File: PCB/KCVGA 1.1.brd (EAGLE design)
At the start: 50 x 50 mm, 61 parts, among them IC1 M68AW128MND, IC2 74245ADB, IC4 LD117AS12TR, IC5 LD117AS33TR, U1 XC3S50ATQ144, U2 PIC32MX250F128B_I_SS, U3 PIC32MX270F256D, X1 D-SUB15, X2 MINI-USB

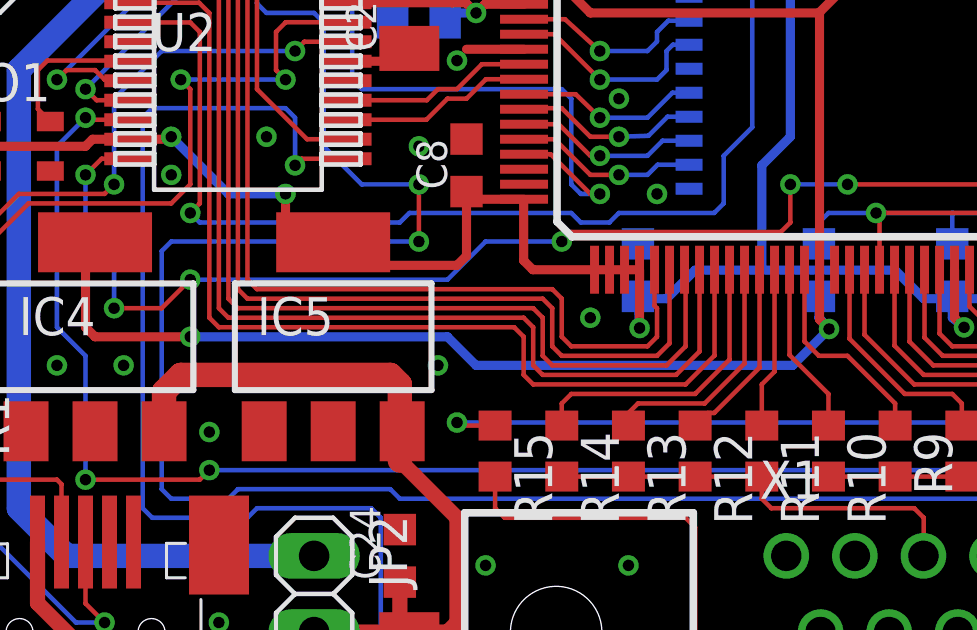
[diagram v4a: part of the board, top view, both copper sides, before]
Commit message: added LDO output caps added Eagle3d files
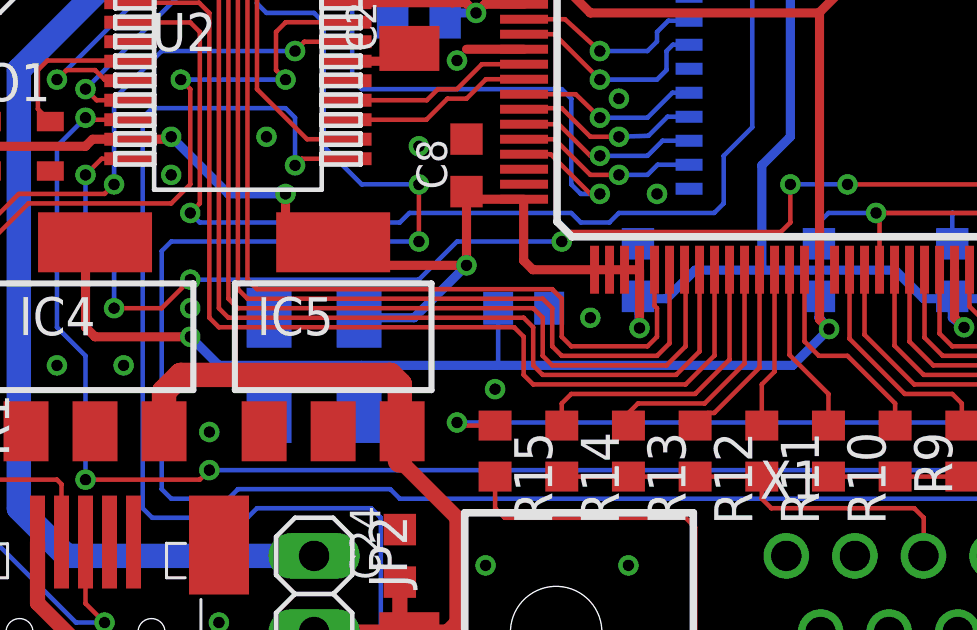
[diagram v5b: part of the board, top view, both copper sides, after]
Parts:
- added C25, C26: 10u, rcl:C1206K
- added R22: 120, rcl:R0603
- IC4: value LD117AS12TR -> LD117AS12
- IC5: value LD117AS33TR -> LD117AS33
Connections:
- net 3V3: now also C26.1
- net GND: now also C25.2, C26.2, R22.1
- net VCCINT: now also C25.1, R22.2
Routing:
- net 3V3: track 237.7 -> 242.2 mm, vias 17 -> 18
- net VCCINT: track 83.1 -> 86.6 mm
- net GND: vias 49 -> 50
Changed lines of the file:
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@@
 <setting verticaltext="up"/>
 </settings>
-<grid distance="12.5" unitdist="mil" unit="mil" style="lines" multiple="1" display="yes" altdistance="1" altunitdist="mil" altunit="mil"/>
+<grid distance="12.5" unitdist="mil" unit="mil" style="lines" multiple="1" display="yes" altdistance="6.25" altunitdist="mil" altunit="mil"/>
 <layers>
 <layer number="1" name="Top" color="4" fill="1" visible="yes" active="yes"/>
@@
 <layer number="19" name="Unrouted" color="6" fill="1" visible="yes" active="yes"/>
 <layer number="20" name="Dimension" color="15" fill="1" visible="yes" active="yes"/>
-<layer number="21" name="tPlace" color="7" fill="1" visible="yes" active="yes"/>
-<layer number="22" name="bPlace" color="7" fill="1" visible="no" active="yes"/>
-<layer number="23" name="tOrigins" color="15" fill="1" visible="yes" active="yes"/>
-<layer number="24" name="bOrigins" color="15" fill="1" visible="no" active="yes"/>
+<layer number="21" name="tPlace" color="7" fill="1" visible="no" active="yes"/>
+<layer number="22" name="bPlace" color="7" fill="1" visible="yes" active="yes"/>
+<layer number="23" name="tOrigins" color="15" fill="1" visible="no" active="yes"/>
+<layer number="24" name="bOrigins" color="15" fill="1" visible="yes" active="yes"/>
 <layer number="25" name="tNames" color="7" fill="1" visible="no" active="yes"/>
 <layer number="26" name="bNames" color="7" fill="1" visible="no" active="yes"/>
@@
 <layer number="49" name="Reference" color="7" fill="1" visible="yes" active="yes"/>
 <layer number="50" name="dxf" color="7" fill="1" visible="no" active="no"/>
-<layer number="51" name="tDocu" color="7" fill="1" visible="yes" active="yes"/>
-<layer number="52" name="bDocu" color="7" fill="1" visible="no" active="yes"/>
+<layer number="51" name="tDocu" color="7" fill="1" visible="no" active="yes"/>
+<layer number="52" name="bDocu" color="7" fill="1" visible="yes" active="yes"/>
 <layer number="90" name="Modules" color="5" fill="1" visible="no" active="no"/>
 <layer number="91" name="Nets" color="2" fill="1" visible="no" active="no"/>
@@
 <element name="R16" library="rcl" package="R0603" value="82" x="48.5775" y="10.795" rot="R270"/>
 <element name="JP3" library="pinhead" package="1X06" value="" x="47.625" y="33.02" rot="R90"/>
-<element name="IC4" library="v-reg" package="SOT223" value="LD117AS12TR" x="6.35" y="14.605"/>
-<element name="IC5" library="v-reg" package="SOT223" value="LD117AS33TR" x="14.2875" y="14.605"/>
+<element name="IC4" library="v-reg" package="SOT223" value="LD117AS12" x="6.35" y="14.605"/>
+<element name="IC5" library="v-reg" package="SOT223" value="LD117AS33" x="14.2875" y="14.605"/>
 <element name="JP2" library="pinhead" package="1X03" value="" x="13.6525" y="4.7625" rot="R270"/>
 <element name="C20" library="rcl" package="C0603K" value="100n" x="1.27" y="20.955" rot="R90"/>
@@
 <element name="JP1" library="pinhead" package="1X06" value="" x="2.54" y="33.02" rot="R270"/>
 <element name="U3" library="PIC32MX270" package="QFP44_10X10MC" value="PIC32MX270F256D" x="6.985" y="-20.0025"/>
+<element name="C25" library="rcl" package="C1206K" value="10u" x="13.6525" y="12.065" rot="MR0"/>
+<element name="C26" library="rcl" package="C1206K" value="10u" x="13.6525" y="15.24" rot="MR0"/>
+<element name="R22" library="rcl" package="R0603" value="120" x="20.6375" y="15.5575" rot="MR0"/>
 </elements>
 <signals>
@@
 <via x="10.4775" y="5.08" extent="1-16" drill="0.381"/>
 <via x="5.08" y="13.6525" extent="1-16" drill="0.381"/>
-<via x="17.78" y="13.6525" extent="1-16" drill="0.381"/>
+<via x="19.685" y="12.85875" extent="1-16" drill="0.381"/>
 <via x="22.86" y="15.24" extent="1-16" drill="0.381"/>
 <via x="2.54" y="23.495" extent="1-16" drill="0.381"/>
@@
 <via x="48.895" y="6.985" extent="1-16" drill="0.381"/>
 <via x="48.895" y="2.54" extent="1-16" drill="0.381"/>
+<contactref element="C26" pad="2"/>
+<contactref element="C25" pad="2"/>
+<contactref element="R22" pad="1"/>
+<via x="9.525" y="15.5575" extent="1-16" drill="0.381"/>
 </signal>
 <signal name="VCCINT">
@@
 <wire x1="6.35" y1="14.605" x2="9.525" y2="14.605" width="0.3048" layer="1"/>
 <via x="9.525" y="14.605" extent="1-16" drill="0.381"/>
-<wire x1="9.525" y1="14.605" x2="18.0975" y2="14.605" width="0.3048" layer="16"/>
-<wire x1="18.0975" y1="14.605" x2="19.05" y2="13.6525" width="0.3048" layer="16"/>
-<wire x1="19.05" y1="13.6525" x2="29.605" y2="13.6525" width="0.3048" layer="16"/>
+<wire x1="9.525" y1="14.605" x2="10.4775" y2="13.6525" width="0.3048" layer="16"/>
+<wire x1="10.4775" y1="13.6525" x2="15.24" y2="13.6525" width="0.3048" layer="16"/>
+<wire x1="15.24" y1="13.6525" x2="19.685" y2="13.6525" width="0.3048" layer="16"/>
+<wire x1="19.685" y1="13.6525" x2="29.605" y2="13.6525" width="0.3048" layer="16"/>
 <wire x1="29.605" y1="13.6525" x2="30.8175" y2="14.865" width="0.3048" layer="16"/>
+<contactref element="C25" pad="1"/>
+<contactref element="R22" pad="2"/>
+<wire x1="15.1525" y1="12.065" x2="15.1525" y2="13.565" width="0.3048" layer="16"/>
+<wire x1="15.1525" y1="13.565" x2="15.24" y2="13.6525" width="0.1524" layer="16"/>
+<wire x1="19.7875" y1="15.5575" x2="19.7875" y2="13.755" width="0.1524" layer="16"/>
+<wire x1="19.7875" y1="13.755" x2="19.685" y2="13.6525" width="0.1524" layer="16"/>
 </signal>
 <signal name="3V3">
@@
 <wire x1="23.495" y1="37.7825" x2="24.4475" y2="38.735" width="0.3048" layer="16"/>
 <wire x1="24.4475" y1="38.735" x2="27.065" y2="38.735" width="0.3048" layer="16"/>
-<wire x1="18.7325" y1="19.445" x2="18.7325" y2="17.30375" width="0.3048" layer="1"/>
-<wire x1="18.7325" y1="17.30375" x2="18.415" y2="16.98625" width="0.3048" layer="1"/>
-<wire x1="18.415" y1="16.98625" x2="15.05625" y2="16.98625" width="0.3048" layer="1"/>
+<wire x1="18.7325" y1="19.445" x2="18.7325" y2="16.98625" width="0.3048" layer="1"/>
+<wire x1="18.7325" y1="16.98625" x2="15.05625" y2="16.98625" width="0.3048" layer="1"/>
 <wire x1="15.05625" y1="16.98625" x2="14.2875" y2="17.755" width="0.3048" layer="1"/>
 <wire x1="37.465" y1="15.875" x2="38.0925" y2="15.875" width="0.3048" layer="16"/>
@@
 <wire x1="10.4775" y1="41.275" x2="10.795" y2="40.9575" width="0.1524" layer="1"/>
 <wire x1="10.795" y1="40.9575" x2="10.795" y2="38.6575" width="0.1524" layer="1"/>
+<contactref element="C26" pad="1"/>
+<wire x1="15.1525" y1="15.24" x2="16.98625" y2="15.24" width="0.3048" layer="16"/>
+<wire x1="16.98625" y1="15.24" x2="18.7325" y2="16.98625" width="0.3048" layer="16"/>
+<via x="18.7325" y="16.98625" extent="1-16" drill="0.381"/>
 </signal>
 <signal name="KC_CLK">
@@
 <wire x1="22.225" y1="18.0975" x2="21.9075" y2="17.78" width="0.1524" layer="1"/>
 <via x="21.9075" y="17.78" extent="1-16" drill="0.381"/>
-<wire x1="21.9075" y1="17.78" x2="19.3675" y2="17.78" width="0.1524" layer="16"/>
-<wire x1="19.3675" y1="17.78" x2="18.0975" y2="16.51" width="0.1524" layer="16"/>
-<wire x1="18.0975" y1="16.51" x2="9.525" y2="16.51" width="0.1524" layer="16"/>
+<wire x1="21.9075" y1="17.78" x2="18.415" y2="17.78" width="0.1524" layer="16"/>
+<wire x1="18.415" y1="17.78" x2="17.145" y2="16.51" width="0.1524" layer="16"/>
+<wire x1="17.145" y1="16.51" x2="9.525" y2="16.51" width="0.1524" layer="16"/>
 <via x="9.525" y="16.51" extent="1-16" drill="0.381"/>
 <wire x1="9.525" y1="16.51" x2="8.5725" y2="15.5575" width="0.1524" layer="1"/>

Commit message: Finished silk screen
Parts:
- removed JP2: (no value), pinhead:1X03
- removed U1: XC3S50ATQ144, xilinx_devices_V6:TQ144
- removed U2: PIC32MX250F128B_I_SS, PIC32MX270:SSOP28_MC
- removed U3: PIC32MX270F256D, PIC32MX270:QFP44_10X10MC
- added IC3: M68AW128MND, st-microelectronics:TSOP44-II
- added IC6: 74245ADB, 74xx-eu:SSOP20D8
- added X3: MINI-USB, con-cypressindustries:32005-301
- added X4: (no value), jumper:JP6Q
- C22: value 10u -> 100n; device rcl:C1206K -> rcl:C0603K
- C24: value 100n -> 10u; device rcl:C0603K -> rcl:C1206K
- IC1: value M68AW128MND -> XC3S50ATQ144; device st-microelectronics:TSOP44-II -> xilinx_devices_V6:TQ144
- IC2: value 74245ADB -> PIC32MX250F128; device 74xx-eu:SSOP20D8 -> PIC32MX270:SSOP28_MC
- X2: value MINI-USB -> (none); device con-cypressindustries:32005-301 -> pinhead:1X03
- moved C22 18.4 mm to (16.5, 7.30)
- moved C24 18.4 mm to (16.8, 25.7)
- moved R18 12.7 mm to (30.2, 16.8), flipped to the bottom
- moved IC2 11.6 mm to (11.1, 24.8)
- moved X2 7.62 mm to (13.7, 4.76), turned to 270 degrees
- moved R16 5.72 mm to (42.9, 10.8)
- moved R3 5.08 mm to (41.3, 10.8)
- moved R4 4.45 mm to (39.7, 10.8)
- moved R20 4.41 mm to (42.7, 20.3), flipped to the bottom, turned to 90 degrees
- moved LED2 4.32 mm to (42.9, 15.2), turned to 270 degrees
- moved R5 3.81 mm to (38.1, 10.8)
- moved R6 3.17 mm to (36.5, 10.8)
- moved R7 2.54 mm to (34.9, 10.8)
- moved R15 2.54 mm to (22.2, 10.8)
- moved C16 1.93 mm to (42.9, 24.4), flipped to the bottom
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- renumbered JP1 to X6, JP3 to X5, SV1 to X7
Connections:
- removed net AVDD: U3.17
- removed net AVSS: U3.16
- removed net FPGA_CLK: U1.P127, U2.10
- removed net VBUS: U3.42
- removed net VCAP: U3.7
- removed net VDD: U3.40
- removed net VDD_2: U3.28
- removed net VSS: U3.39
- removed net VSS_2: U3.6
- removed net VSS_3: U3.29
- new net JP0: IC1.P70, X4.2
- new net JP1: IC1.P69, X4.4
- new net JP2: IC1.P68, X4.6
- new net JP3: IC1.P75, X4.8
- new net JP4: IC1.P76, X4.10
- new net JP5: IC1.P77, X4.12
- net !BHE: now also IC1.P7, IC3.40; no longer IC1.40, U1.P7
- net !BLE: now also IC1.P8, IC3.39; no longer IC1.39, U1.P8
- net !CE: now also IC1.P99, IC3.6; no longer IC1.6, U1.P99
- net !FPGA_RESET: now also IC1.P19, IC2.10; no longer U1.P19
- net !INIT_B: now also IC1.P67, IC2.14; no longer U1.P67, U2.14
- net !OE: now also IC1.P6, IC3.41; no longer IC1.41, U1.P6
- net !PMRD: now also IC1.P33, IC2.24; no longer U1.P33, U2.24
- net !PMWR: now also IC1.P140, IC2.7; no longer U1.P140, U2.7
- net !PROG_B: now also IC1.P144, IC2.11; no longer U1.P144, U2.11
- net !RESET: now also IC2.1; no longer U2.1
- net !WE: now also IC1.P85, IC3.17; no longer IC1.17, U1.P85
- net +5V: now also C22.1, X2.2; no longer C24.1, JP2.2
- net 3V3: now also IC1.P108, IC1.P119, IC1.P133, IC1.P136, IC1.P14, IC1.P143, IC1.P23, IC1.P36, IC1.P37, IC1.P38, IC1.P39, IC1.P40, IC1.P61, IC1.P66, IC1.P86, IC1.P95, IC2.13, IC2.23, IC2.28, IC3.11, IC3.33, IC6.1, IC6.20; no longer IC1.11, IC1.33, IC2.1, IC2.20, U1.P108, U1.P119, U1.P133, U1.P136, U1.P14, U1.P143, U1.P23, U1.P36, U1.P37, U1.P38, U1.P39, U1.P40, U1.P61, U1.P66, U1.P86, U1.P95, U2.13, U2.23, U2.28
- net A0: now also IC1.P101, IC3.5; no longer IC1.5, U1.P101
- net A1: now also IC1.P102, IC3.4; no longer IC1.4, U1.P102
- net A10: now also IC1.P31, IC3.25; no longer IC1.25, U1.P31
- net A11: now also IC1.P32, IC3.24; no longer IC1.24, U1.P32
- net A12: now also IC1.P78, IC3.22; no longer IC1.22, U1.P78
- net A13: now also IC1.P79, IC3.21; no longer IC1.21, U1.P79
- net A14: now also IC1.P82, IC3.20; no longer IC1.20, U1.P82
- net A15: now also IC1.P83, IC3.19; no longer IC1.19, U1.P83
- net A16: now also IC1.P84, IC3.18; no longer IC1.18, U1.P84
- net A2: now also IC1.P103, IC3.3; no longer IC1.3, U1.P103
- net A3: now also IC1.P104, IC3.2; no longer IC1.2, U1.P104
- net A4: now also IC1.P105, IC3.1; no longer IC1.1, U1.P105
- net A5: now also IC1.P3, IC3.44; no longer IC1.44, U1.P3
- net A6: now also IC1.P4, IC3.43; no longer IC1.43, U1.P4
- net A7: now also IC1.P5, IC3.42; no longer IC1.42, U1.P5
- net A8: now also IC1.P29, IC3.27; no longer IC1.27, U1.P29
- net A9: now also IC1.P30, IC3.26; no longer IC1.26, U1.P30
- net CLK_32M: now also IC1.P127, IC2.9; no longer U2.9
- net D0: now also IC1.P98, IC3.7; no longer IC1.7, U1.P98
- net D1: now also IC1.P96, IC3.8; no longer IC1.8, U1.P96
- net D10: now also IC1.P21, IC3.31; no longer IC1.31, U1.P21
- net D11: now also IC1.P20, IC3.32; no longer IC1.32, U1.P20
- net D12: now also IC1.P15, IC3.35; no longer IC1.35, U1.P15
- net D13: now also IC1.P13, IC3.36; no longer IC1.36, U1.P13
- net D14: now also IC1.P12, IC3.37; no longer IC1.37, U1.P12
- net D15: now also IC1.P10, IC3.38; no longer IC1.38, U1.P10
- net D2: now also IC1.P93, IC3.9; no longer IC1.9, U1.P93
- net D3: now also IC1.P92, IC3.10; no longer IC1.10, U1.P92
- net D4: now also IC1.P91, IC3.13; no longer IC1.13, U1.P91
- net D5: now also IC1.P90, IC3.14; no longer IC1.14, U1.P90
- net D6: now also IC1.P88, IC3.15; no longer IC1.15, U1.P88
- net D7: now also IC1.P87, IC3.16; no longer IC1.16, U1.P87
- net D8: now also IC1.P25, IC3.29; no longer IC1.29, U1.P25
- net D9: now also IC1.P24, IC3.30; no longer IC1.30, U1.P24
- net DONE: now also IC1.P73; no longer U1.P73
- net FPGA_CCLK: now also IC1.P72, IC2.25; no longer U1.P72, U2.25
- net FPGA_DIN: now also IC1.P71, IC2.12; no longer U1.P71, U2.12
- net GND: now also IC1.P100, IC1.P106, IC1.P118, IC1.P128, IC1.P137, IC1.P17, IC1.P26, IC1.P34, IC1.P56, IC1.P65, IC1.P74, IC1.P81, IC1.P89, IC1.P9, IC2.27, IC2.8, IC3.12, IC3.34, IC6.10, IC6.19, X3.5, X3.M1, X3.M2, X3.M3, X3.M4, X4.1, X4.11, X4.3, X4.5, X4.7, X4.9; no longer IC1.12, IC1.34, IC2.10, U1.P100, U1.P106, U1.P118, U1.P128, U1.P137, U1.P17, U1.P26, U1.P34, U1.P56, U1.P65, U1.P74, U1.P81, U1.P89, U1.P9, U2.19, U2.27, U2.8, X2.5, X2.M1, X2.M2, X2.M3, X2.M4
- net KC_B: now also IC1.P132, IC6.4; no longer IC2.4, U1.P132
- net KC_CLK: now also IC1.P142, IC6.9; no longer IC2.9, U1.P142
- net KC_EX: now also IC1.P131, IC6.3; no longer IC2.3, U1.P131
- net KC_EZ: now also IC1.P130, IC6.2; no longer IC2.2, U1.P130
- net KC_G: now also IC1.P134, IC6.5; no longer IC2.5, U1.P134
- net KC_HSYNC: now also IC1.P139, IC6.8; no longer IC2.8, U1.P139
- net KC_R: now also IC1.P135, IC6.6; no longer IC2.6, U1.P135
- net KC_VSYNC: now also IC1.P138, IC6.7; no longer IC2.7, U1.P138
- net N$1: now also IC2.15, X2.3, X3.1; no longer JP2.3, U2.15, X2.1
- net N$11: now also IC2.22; no longer U2.22
- net N$12: now also IC2.21; no longer U2.21
- net N$13: now also X3.2; no longer X2.2
- net N$14: now also X3.3; no longer X2.3
- net N$16: now also C24.1, IC2.20; no longer C22.1, U2.20
- net N$2: now also IC6.18; no longer IC2.18
- net N$20: now also X2.1; no longer JP2.1
- net N$22: now also IC2.26; no longer U2.26
- net N$3: now also IC6.17; no longer IC2.17
- net N$4: now also IC6.16; no longer IC2.16
- net N$5: now also IC6.15; no longer IC2.15
- net N$6: now also IC6.14; no longer IC2.14
- net N$7: now also IC6.13; no longer IC2.13
- net N$8: now also IC6.12; no longer IC2.12
- net N$9: now also IC6.11; no longer IC2.11
- net PMD0: now also IC1.P43, IC2.4; no longer U1.P43, U2.4
- net PMD1: now also IC1.P44, IC2.5; no longer U1.P44, U2.5
- net PMD2: now also IC1.P45, IC2.6; no longer U1.P45, U2.6
- net PMD3: now also IC1.P27, IC2.18; no longer U1.P27, U2.18
- net PMD4: now also IC1.P28, IC2.17; no longer U1.P28, U2.17
- net PMD5: now also IC1.P18, IC2.16; no longer U1.P18, U2.16
- net PMD6: now also IC1.P42, IC2.3; no longer U1.P42, U2.3
- net PMD7: now also IC1.P41, IC2.2; no longer U1.P41, U2.2
- net TCK: now also IC1.P109; no longer U1.P109
- net TDI: now also IC1.P2; no longer U1.P2
- net TDO: now also IC1.P107; no longer U1.P107
- net TMS: now also IC1.P1; no longer U1.P1
- net VCCINT: now also IC1.P122, IC1.P22, IC1.P52, IC1.P94; no longer U1.P122, U1.P22, U1.P52, U1.P94
- net VGA_B0: now also IC1.P46; no longer U1.P46
- net VGA_B1: now also IC1.P47; no longer U1.P47
- net VGA_B2: now also IC1.P48; no longer U1.P48
- net VGA_B3: now also IC1.P49; no longer U1.P49
- net VGA_G0: now also IC1.P50; no longer U1.P50
- net VGA_G1: now also IC1.P51; no longer U1.P51
- net VGA_G2: now also IC1.P54; no longer U1.P54
- net VGA_G3: now also IC1.P55; no longer U1.P55
- net VGA_HSYNC: now also IC1.P64; no longer U1.P64
- net VGA_R0: now also IC1.P57; no longer U1.P57
- net VGA_R1: now also IC1.P58; no longer U1.P58
- net VGA_R2: now also IC1.P59; no longer U1.P59
- net VGA_R3: now also IC1.P60; no longer U1.P60
- net VGA_VSYNC: now also IC1.P62; no longer U1.P62
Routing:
- net FPGA_CLK: track 43.3 -> 0.00 mm, vias 2 -> 0
- net CLK_32M: track 5.08 -> 44.6 mm, vias 0 -> 2
- net !FPGA_RESET: track 0.00 -> 16.1 mm, vias 0 -> 2
- net JP0: track 0.00 -> 13.7 mm
- net JP1: track 0.00 -> 12.2 mm
- net JP2: track 0.00 -> 10.3 mm
- net VGA_HSYNC: track 16.7 -> 11.0 mm
- net N$21: track 2.11 -> 7.62 mm, vias 0 -> 1
- net N$10: track 24.8 -> 19.4 mm
- net VGA_R3: track 16.6 -> 11.5 mm
- net JP5: track 0.00 -> 5.07 mm
- net JP3: track 0.00 -> 4.67 mm
- net VGA_R2: track 14.8 -> 10.3 mm
- net 3V3: track 242.2 -> 246.4 mm, vias 18 -> 17
- net VGA_R1: track 13.0 -> 9.15 mm
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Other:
- board text added: "KCVGA v1.1"
- board text added: "bot"
- board text added: "thoralt@googlemail.com"
- board text added: "top"
- board text removed: "1"

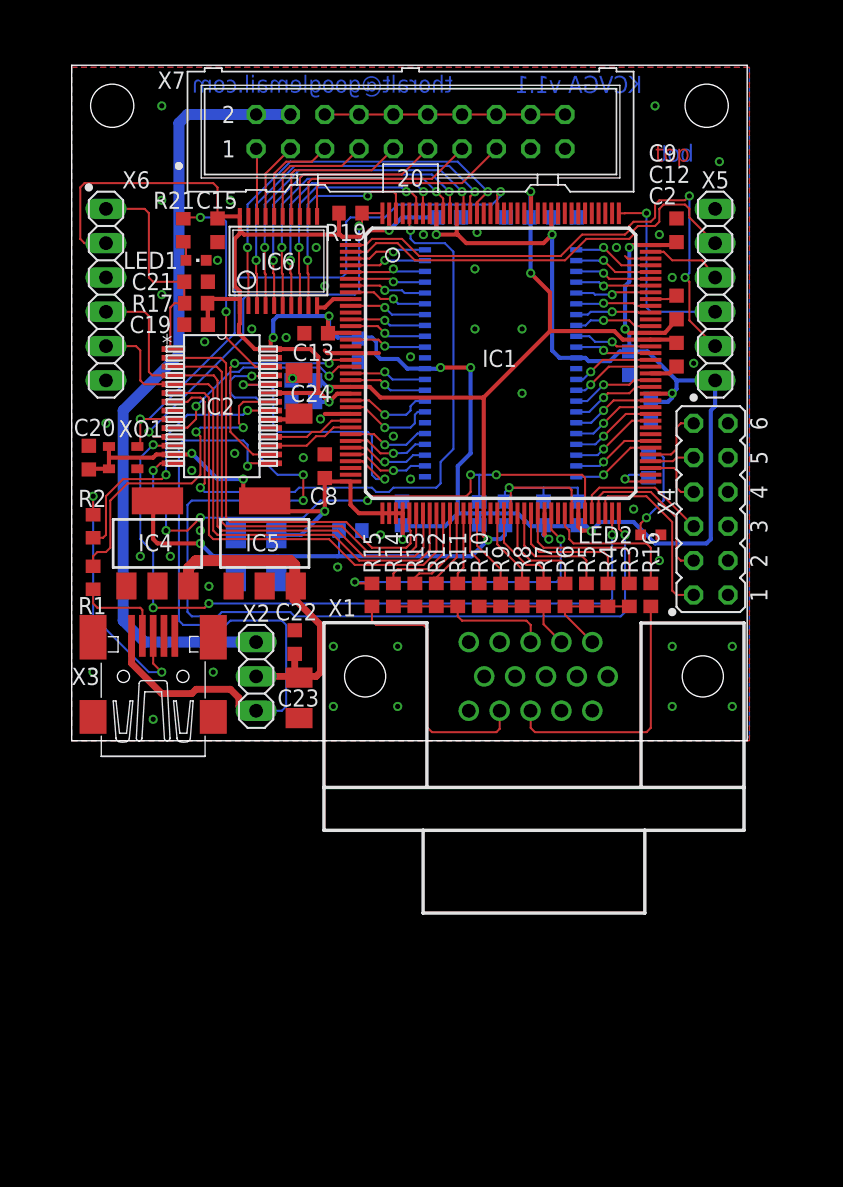
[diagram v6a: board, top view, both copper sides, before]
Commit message: optimized silkscreen
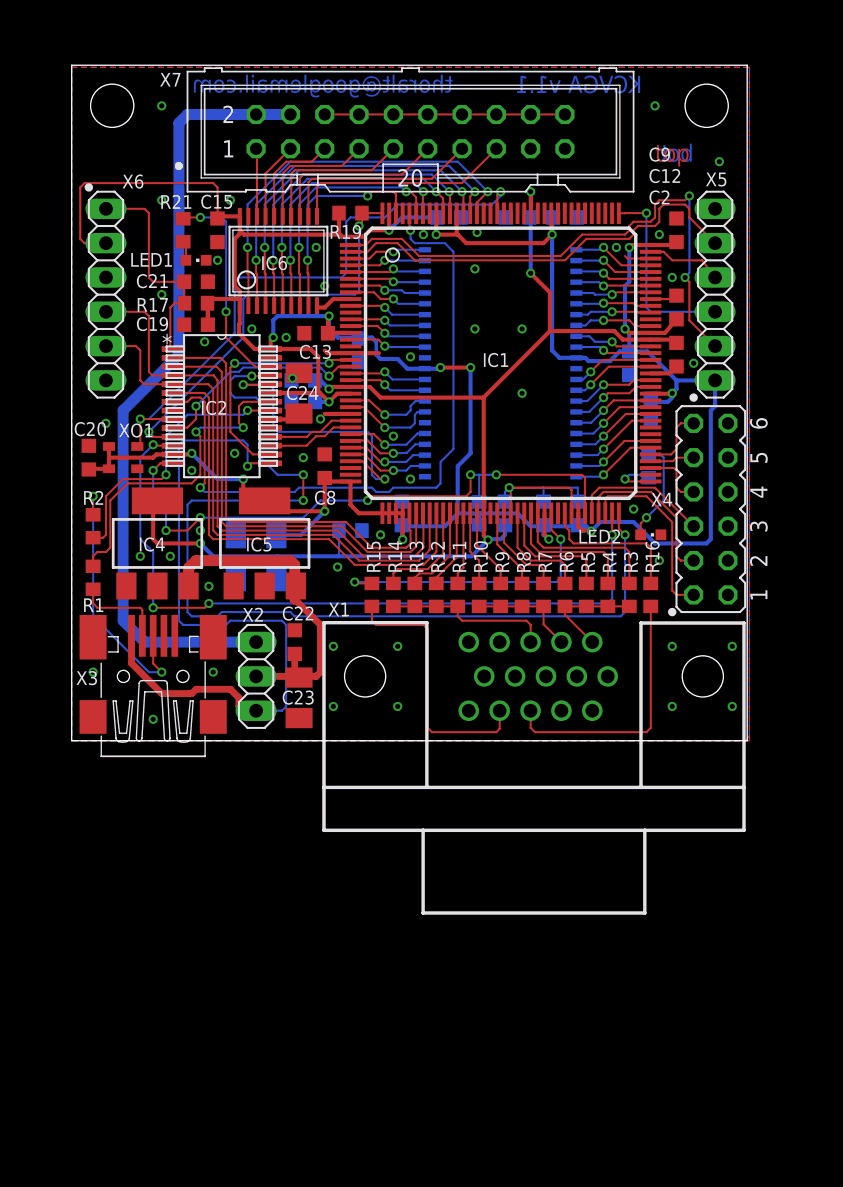
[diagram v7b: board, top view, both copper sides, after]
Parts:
- IC4: value LD117AS12 -> AP1117-1.2
- IC5: value LD117AS33 -> AP1117-3.3
